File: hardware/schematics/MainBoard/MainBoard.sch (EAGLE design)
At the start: 17 parts

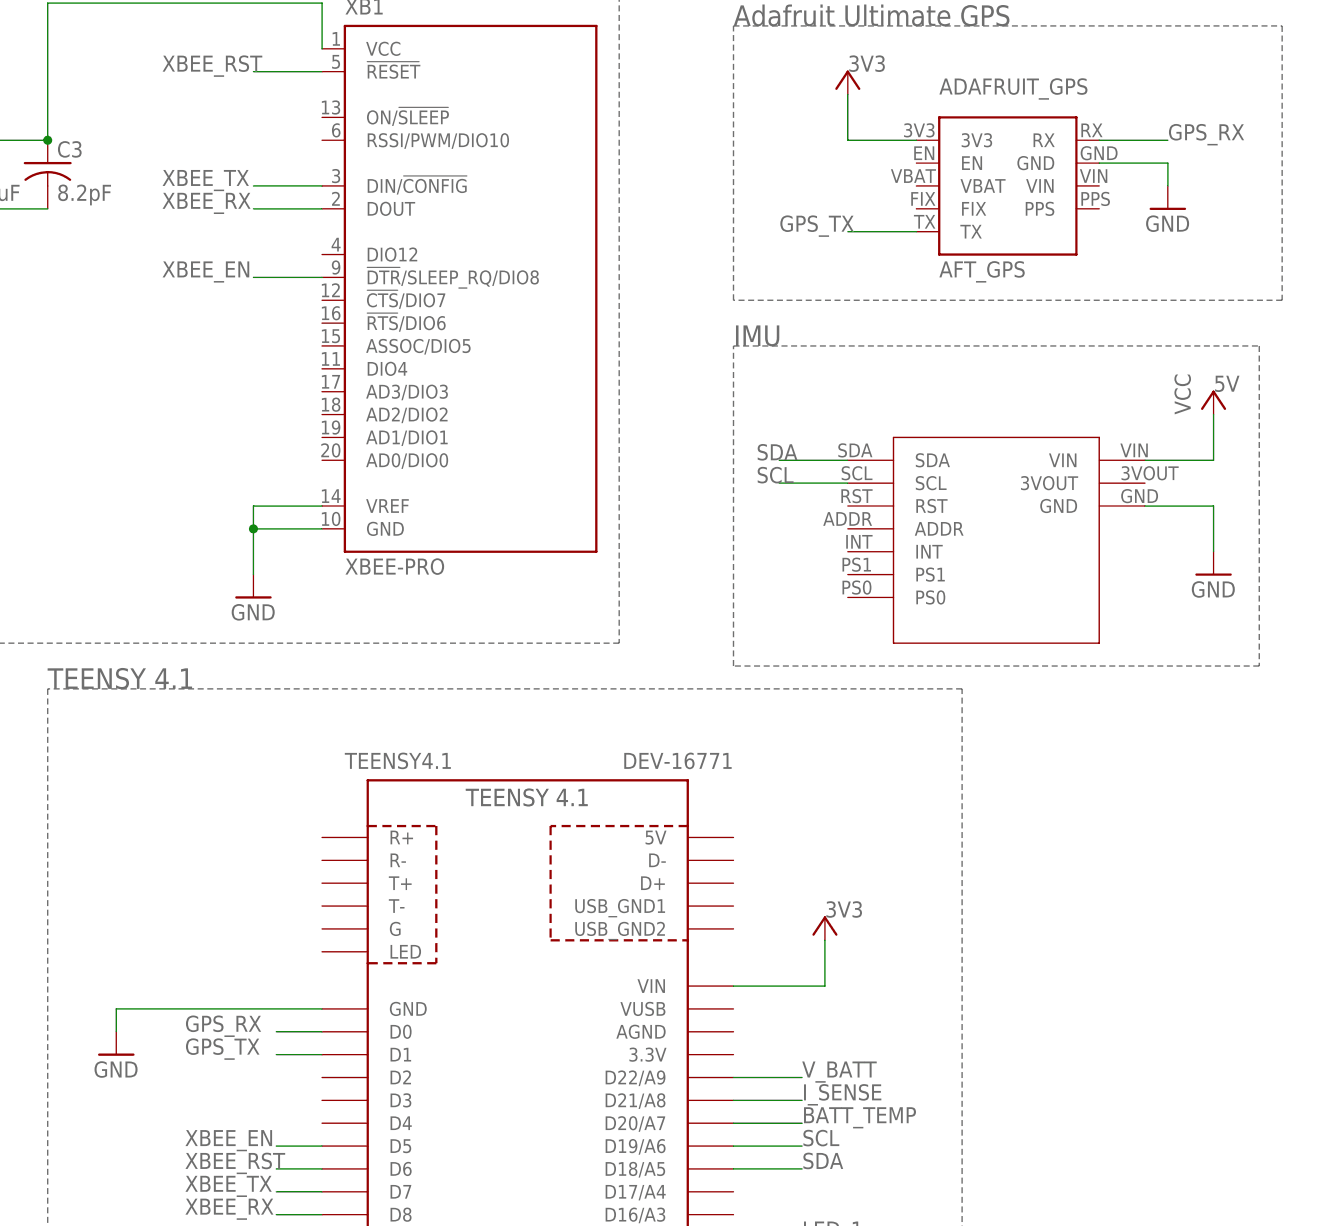
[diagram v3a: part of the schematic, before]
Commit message: Fixed TX/RX pins for GPS and Xbee
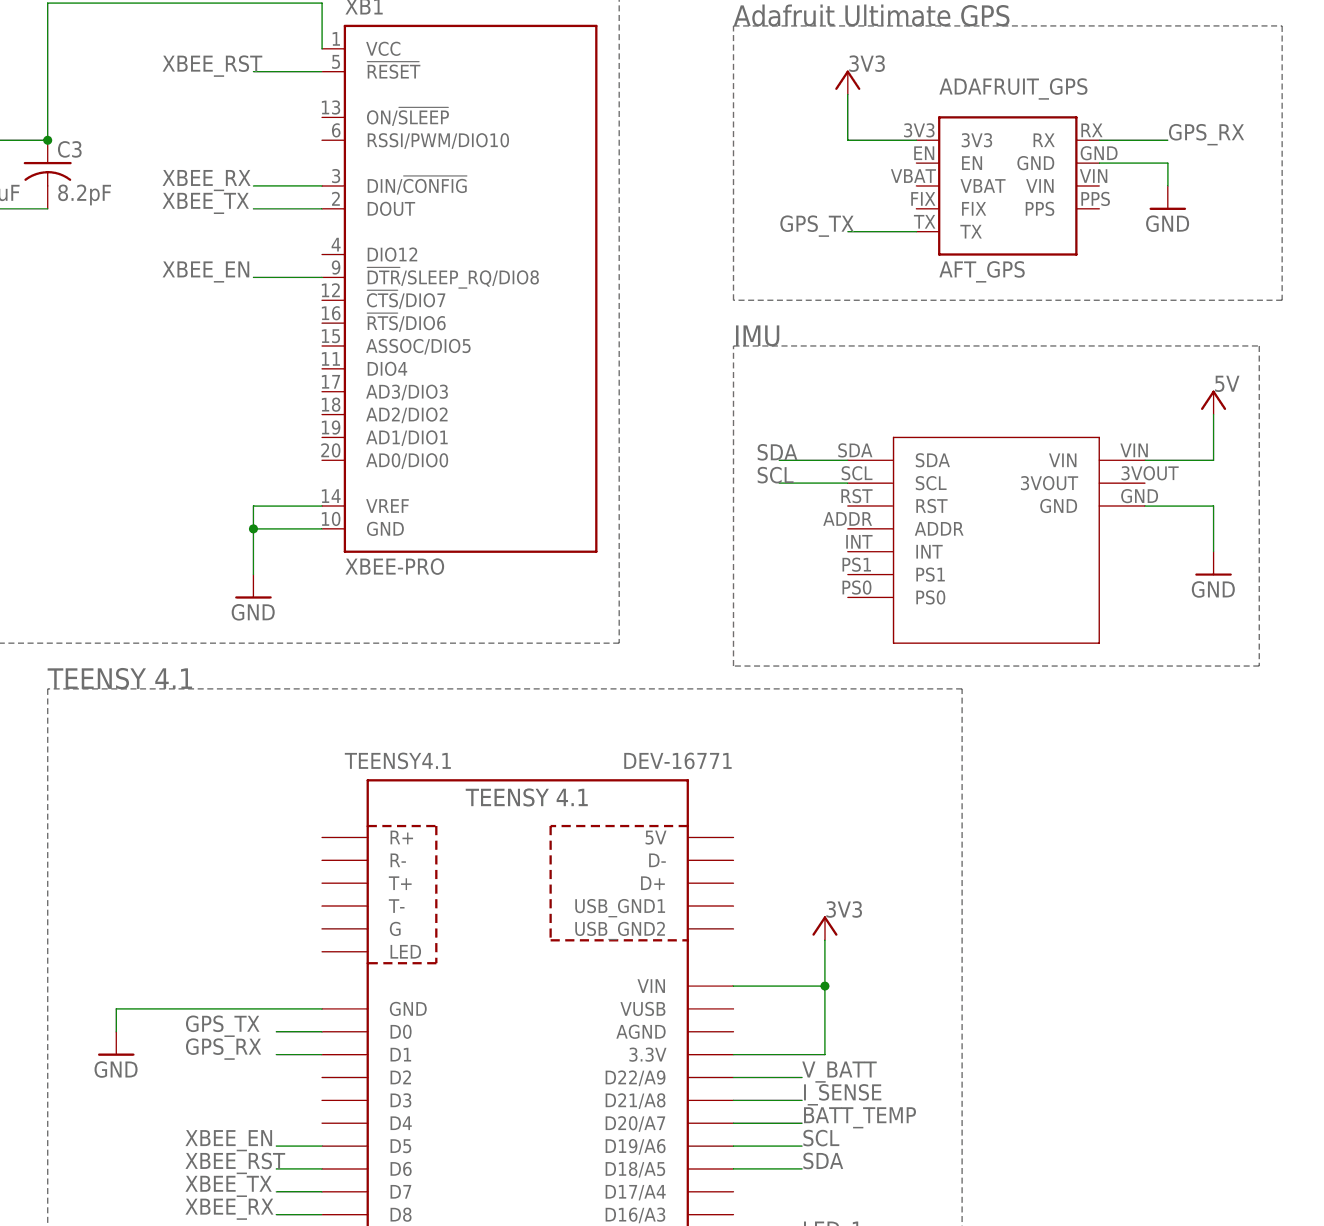
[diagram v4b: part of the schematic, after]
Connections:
- net 3V3: now also TEENSY4.1.3.3V@1
- net GPS_RX: now also TEENSY4.1.D1; no longer TEENSY4.1.D0
- net GPS_TX: now also TEENSY4.1.D0; no longer TEENSY4.1.D1
- net XBEE_RX: now also XB1.DIN/!CONFIG; no longer XB1.DOUT
- net XBEE_TX: now also XB1.DOUT; no longer XB1.DIN/!CONFIG
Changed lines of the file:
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@@
 </instance>
 <instance part="U$1" gate="G$1" x="91.44" y="-30.48" smashed="yes"/>
-<instance part="P+4" gate="VCC" x="127" y="-25.4" smashed="yes">
-<attribute name="VALUE" x="124.46" y="-27.94" size="1.778" layer="96" rot="R90"/>
-</instance>
+<instance part="P+4" gate="VCC" x="127" y="-25.4" smashed="yes"/>
 <instance part="GND4" gate="1" x="127" y="-45.72" smashed="yes">
 <attribute name="VALUE" x="124.46" y="-48.26" size="1.778" layer="96"/>
@@
 <pinref part="P+3" gate="VCC" pin="VCC"/>
 <label x="83.82" y="-83.82" size="1.778" layer="95"/>
+<pinref part="TEENSY4.1" gate="G$1" pin="3.3V@1"/>
+<wire x1="73.66" y1="-99.06" x2="83.82" y2="-99.06" width="0.1524" layer="91"/>
+<wire x1="83.82" y1="-99.06" x2="83.82" y2="-91.44" width="0.1524" layer="91"/>
+<junction x="83.82" y="-91.44"/>
 </segment>
 <segment>
@@
 </segment>
 <segment>
+<pinref part="TEENSY4.1" gate="G$1" pin="D0"/>
+<wire x1="27.94" y1="-96.52" x2="22.86" y2="-96.52" width="0.1524" layer="91"/>
+<label x="12.7" y="-96.52" size="1.778" layer="95"/>
+</segment>
+</net>
+<net name="GPS_RX" class="0">
+<segment>
+<pinref part="ADAFRUIT_GPS" gate="G$1" pin="RX"/>
+<wire x1="114.3" y1="2.54" x2="121.92" y2="2.54" width="0.1524" layer="91"/>
+<label x="121.92" y="2.54" size="1.778" layer="95"/>
+</segment>
+<segment>
 <pinref part="TEENSY4.1" gate="G$1" pin="D1"/>
 <wire x1="27.94" y1="-99.06" x2="22.86" y2="-99.06" width="0.1524" layer="91"/>
 <label x="12.7" y="-99.06" size="1.778" layer="95"/>
-</segment>
-</net>
-<net name="GPS_RX" class="0">
-<segment>
-<pinref part="ADAFRUIT_GPS" gate="G$1" pin="RX"/>
-<wire x1="114.3" y1="2.54" x2="121.92" y2="2.54" width="0.1524" layer="91"/>
-<label x="121.92" y="2.54" size="1.778" layer="95"/>
-</segment>
-<segment>
-<pinref part="TEENSY4.1" gate="G$1" pin="D0"/>
-<wire x1="27.94" y1="-96.52" x2="22.86" y2="-96.52" width="0.1524" layer="91"/>
-<label x="12.7" y="-96.52" size="1.778" layer="95"/>
 </segment>
 </net>
@@
 <net name="XBEE_TX" class="0">
 <segment>
+<pinref part="TEENSY4.1" gate="G$1" pin="D7"/>
+<wire x1="27.94" y1="-114.3" x2="22.86" y2="-114.3" width="0.1524" layer="91"/>
+<label x="12.7" y="-114.3" size="1.778" layer="95"/>
+</segment>
+<segment>
+<wire x1="27.94" y1="-5.08" x2="20.32" y2="-5.08" width="0.1524" layer="91"/>
+<label x="10.16" y="-5.08" size="1.778" layer="95"/>
+<pinref part="XB1" gate="G$1" pin="DOUT"/>
+</segment>
+</net>
+<net name="XBEE_RST" class="0">
+<segment>
+<wire x1="27.94" y1="10.16" x2="20.32" y2="10.16" width="0.1524" layer="91"/>
+<label x="10.16" y="10.16" size="1.778" layer="95"/>
+<pinref part="XB1" gate="G$1" pin="!RESET"/>
+</segment>
+<segment>
+<pinref part="TEENSY4.1" gate="G$1" pin="D6"/>
+<wire x1="27.94" y1="-111.76" x2="22.86" y2="-111.76" width="0.1524" layer="91"/>
+<label x="12.7" y="-111.76" size="1.778" layer="95"/>
+</segment>
+</net>
+<net name="XBEE_RX" class="0">
+<segment>
+<pinref part="TEENSY4.1" gate="G$1" pin="D8"/>
+<wire x1="27.94" y1="-116.84" x2="22.86" y2="-116.84" width="0.1524" layer="91"/>
+<label x="12.7" y="-116.84" size="1.778" layer="95"/>
+</segment>
+<segment>
 <wire x1="27.94" y1="-2.54" x2="20.32" y2="-2.54" width="0.1524" layer="91"/>
 <label x="10.16" y="-2.54" size="1.778" layer="95"/>
 <pinref part="XB1" gate="G$1" pin="DIN/!CONFIG"/>
 </segment>
-<segment>
-<pinref part="TEENSY4.1" gate="G$1" pin="D7"/>
-<wire x1="27.94" y1="-114.3" x2="22.86" y2="-114.3" width="0.1524" layer="91"/>
-<label x="12.7" y="-114.3" size="1.778" layer="95"/>
-</segment>
-</net>
-<net name="XBEE_RST" class="0">
-<segment>
-<wire x1="27.94" y1="10.16" x2="20.32" y2="10.16" width="0.1524" layer="91"/>
-<label x="10.16" y="10.16" size="1.778" layer="95"/>
-<pinref part="XB1" gate="G$1" pin="!RESET"/>
-</segment>
-<segment>
-<pinref part="TEENSY4.1" gate="G$1" pin="D6"/>
-<wire x1="27.94" y1="-111.76" x2="22.86" y2="-111.76" width="0.1524" layer="91"/>
-<label x="12.7" y="-111.76" size="1.778" layer="95"/>
-</segment>
-</net>
-<net name="XBEE_RX" class="0">
-<segment>
-<pinref part="TEENSY4.1" gate="G$1" pin="D8"/>
-<wire x1="27.94" y1="-116.84" x2="22.86" y2="-116.84" width="0.1524" layer="91"/>
-<label x="12.7" y="-116.84" size="1.778" layer="95"/>
-</segment>
-<segment>
-<wire x1="27.94" y1="-5.08" x2="20.32" y2="-5.08" width="0.1524" layer="91"/>
-<label x="10.16" y="-5.08" size="1.778" layer="95"/>
-<pinref part="XB1" gate="G$1" pin="DOUT"/>
-</segment>
-</net>
+</net>
